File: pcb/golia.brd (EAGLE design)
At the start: 41.7 x 33.8 mm, 20 parts, among them IC1 xm64a4u, U1 MCP1825S-3302E/DB, X2 EXT

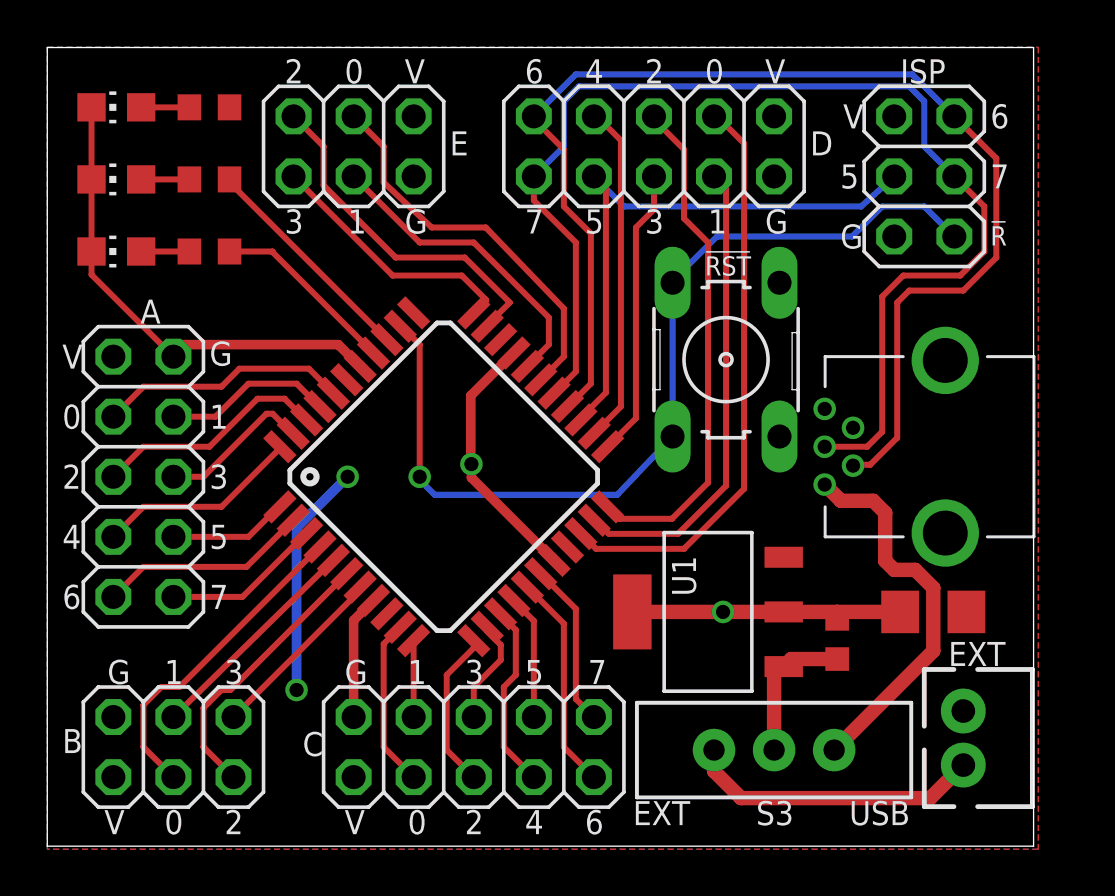
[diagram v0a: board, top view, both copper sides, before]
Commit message: Corrected silk screen and measurement layering
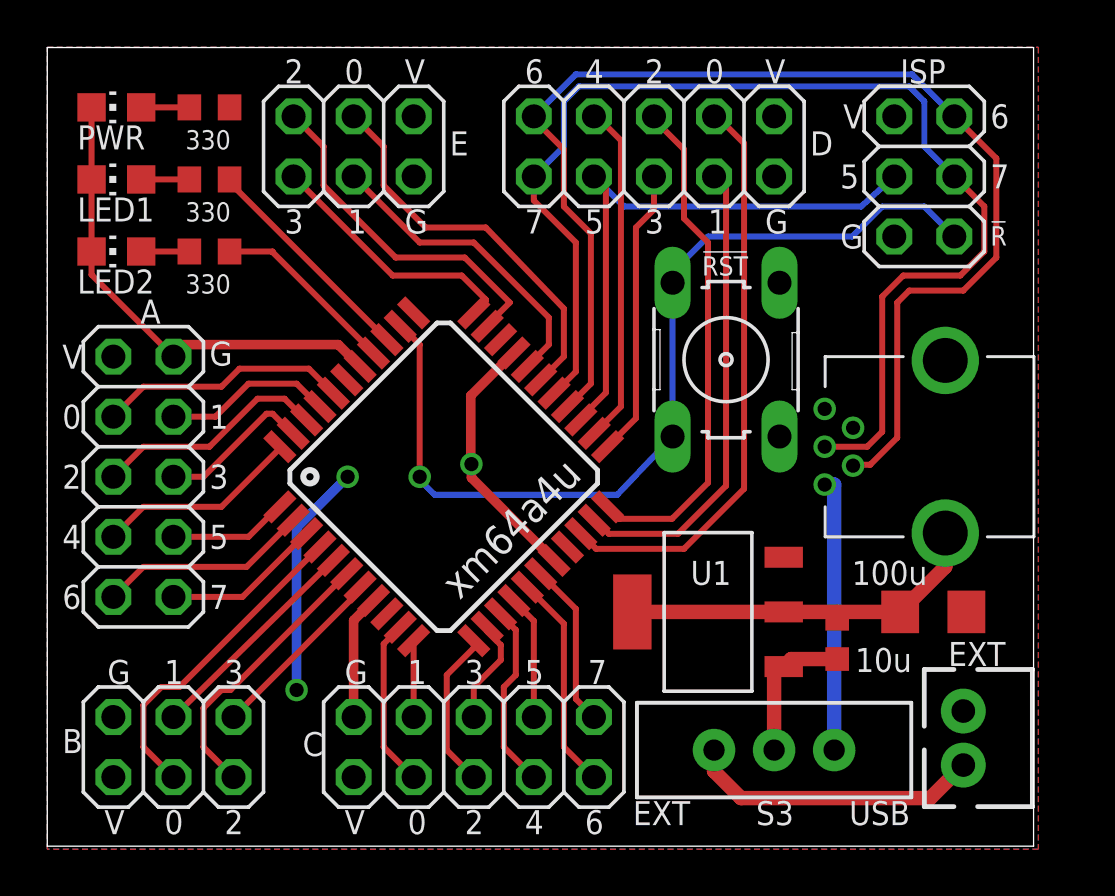
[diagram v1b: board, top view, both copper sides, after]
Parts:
- E: value (none) -> (none)
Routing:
- net N$2: track 16.2 -> 11.6 mm
- net GND: track 48.5 -> 52.7 mm, vias 2 -> 1
